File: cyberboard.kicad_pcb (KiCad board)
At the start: 4 copper layers, 65 x 56.5 mm, 51 parts, among them J1 Conn_01x02, J2 Conn_01x06, J3 5024940670, J4 Lidar, J6 RPi_GPIO, J7 Conn_01x04, J8 Conn_01x03, Q1 AO3400A, Q2 AO3400A, Q3 AO3400A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

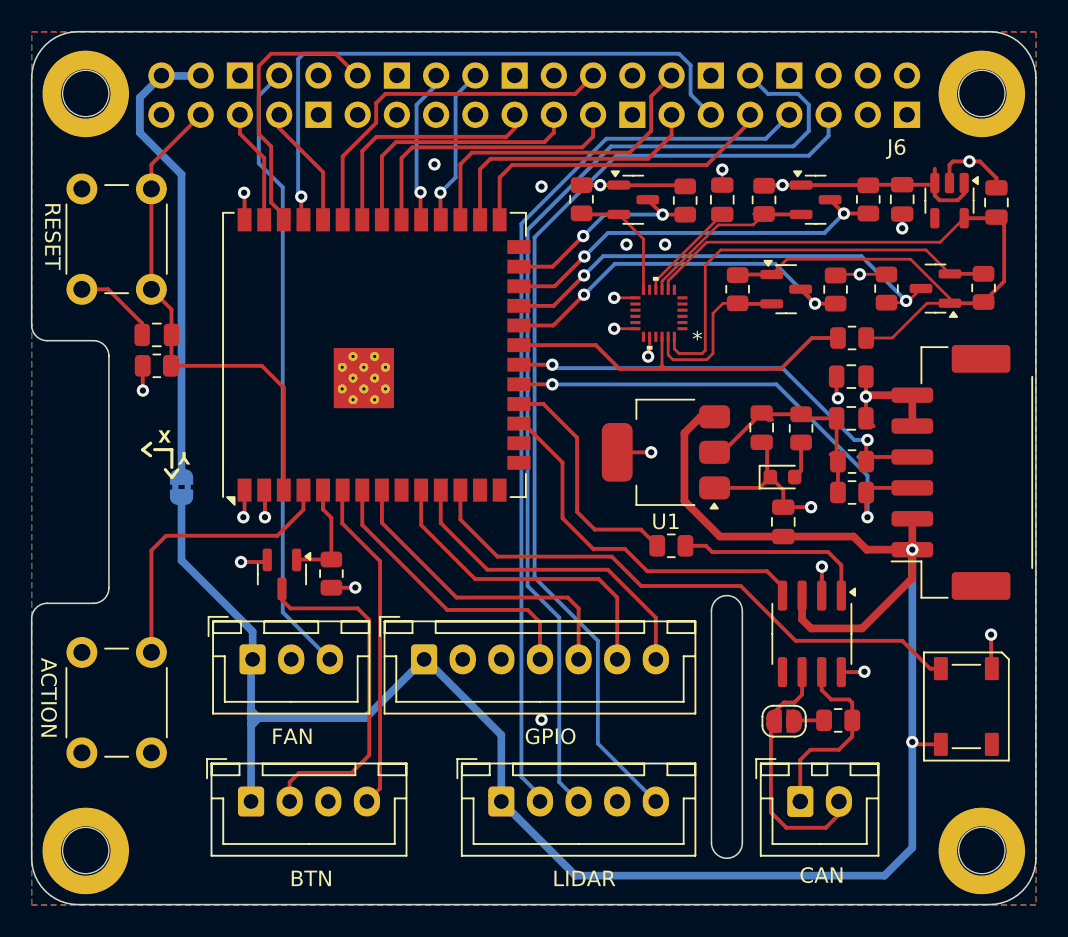
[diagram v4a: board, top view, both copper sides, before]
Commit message: add LED connector and update FAN connector
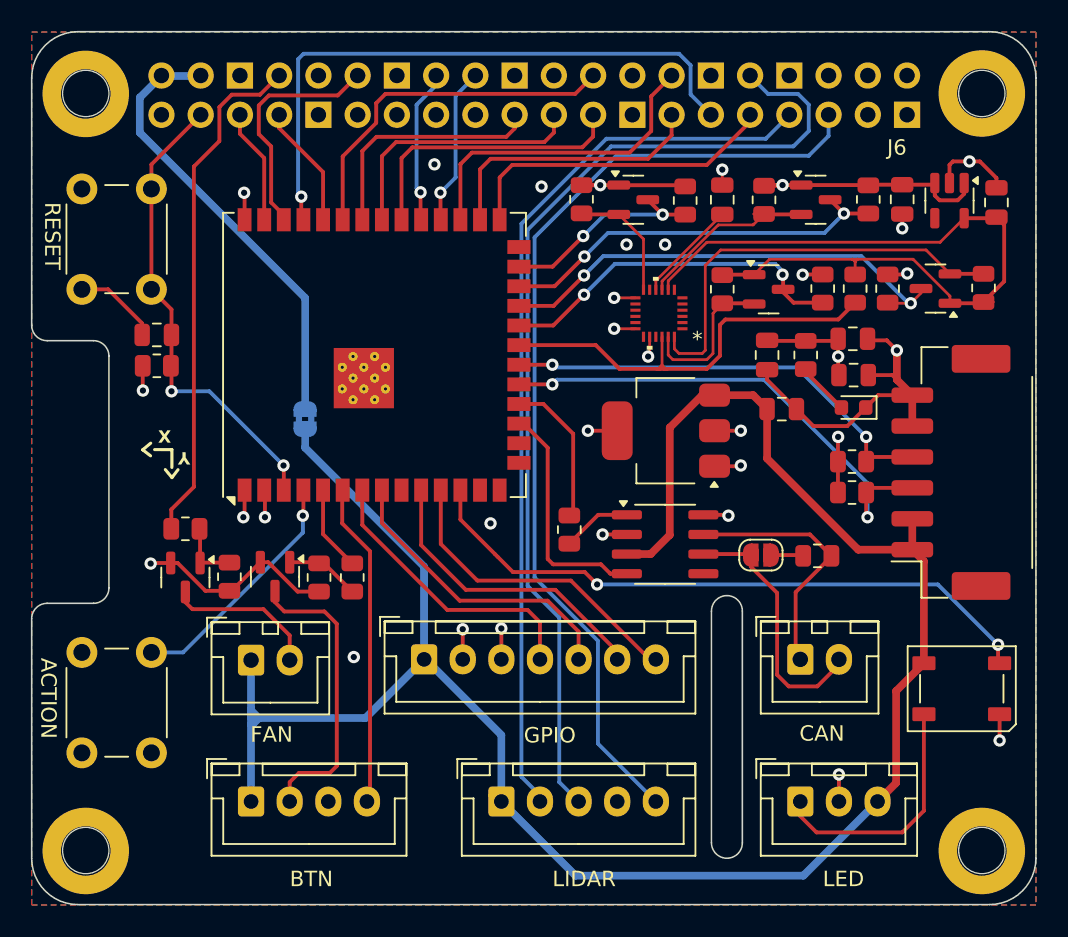
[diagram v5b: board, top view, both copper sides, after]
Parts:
- added J5: Conn_01x03, Connector_JST:JST_XH_B3B-XH-A_1x03_P2.50mm_Vertical, F.Cu at (156.0, 116.8)
- added Q6: AO3400A, Package_TO_SOT_SMD:SOT-23, F.Cu at (116.2, 102.3)
- added R6: 10k, Resistor_SMD:R_0805_2012Metric, F.Cu at (119.1, 102.3)
- added R7: 220, Resistor_SMD:R_0805_2012Metric, F.Cu at (116.2, 99.2)
- added R8: 220, Resistor_SMD:R_0805_2012Metric, F.Cu at (127.0, 102.3)
- J8: footprint Connector_JST:JST_XH_B3B-XH-A_1x03_P2.50mm_Vertical -> Connector_JST:JST_XH_B2B-XH-A_1x02_P2.50mm_Vertical
- moved U2 11.1 mm to (147.3, 100.2), turned to 0 degrees
- moved JP3 10.9 mm to (153.5, 100.9)
- moved R2 10.7 mm to (157.1, 100.9)
- moved J1 9.20 mm to (156.0, 107.6)
- moved JP1 9.13 mm to (124.0, 92.1)
- moved C3 7.30 mm to (154.8, 91.4), turned to 0 degrees
- moved R3 6.68 mm to (141.1, 99.2), turned to 90 degrees
- moved D2 6.44 mm to (159.5, 91.3), turned to 180 degrees
- moved R5 4.76 mm to (156.4, 87.9)
- moved C4 4.71 mm to (153.9, 87.9)
- moved R11 3.21 mm to (159.6, 83.6), turned to -90 degrees
- moved C2 2.80 mm to (159.5, 89.2)
- moved C6 2.45 mm to (159.4, 86.9)
- moved U1 1.40 mm to (147.3, 92.8)
- moved D1 1.19 mm to (166.5, 109.5), turned to 0 degrees
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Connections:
- D1 pad 2: unconnected-(D1-DOUT-Pad2) -> Net-(D1-DOUT)
- J6 pad 8: /FAN -> /FAN_PWM
- J8 pad 2: GND -> Net-(D3-A)
- Q4 pad 1: /BTN_LED -> Net-(Q4-G)
- R4 pad 2: /BTN_LED -> Net-(Q4-G)
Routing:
- net /FAN: track 40.2 -> 0.00 mm
- net /FAN_PWM: track 0.00 -> 33.3 mm
- net GND: track 47.7 -> 65.3 mm, vias 19 -> 21
- net Net-(D1-DOUT): track 0.00 -> 16.2 mm
- net Net-(D3-A): track 0.00 -> 9.90 mm
- net /CAN_RX: track 24.1 -> 15.2 mm
- net Net-(U2-TXD): track 12.6 -> 4.50 mm
- net /CAN_TX: track 15.9 -> 10.0 mm
- net Net-(Q4-G): track 0.00 -> 4.84 mm
- net +3.3V: track 53.0 -> 48.5 mm, vias 8 -> 12
- net /GPIO_LED: track 37.0 -> 41.3 mm, vias 0 -> 2
- net Net-(J1-Pin_1): track 12.3 -> 16.6 mm
- net Net-(Q6-G): track 0.00 -> 4.14 mm
- net +1V8: track 54.5 -> 50.7 mm
- net /BTN_LED_5V: track 22.8 -> 19.2 mm
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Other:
- board text added: "LED"

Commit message: fix pcb layout
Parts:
- added D3: D, Diode_SMD:D_SOD-323, F.Cu at (117.1, 106.4)
- moved R7 11.6 mm to (117.2, 87.6), turned to 90 degrees
- moved J7 0.91 mm to (121.4, 116.9)
- moved J8 0.91 mm to (121.4, 107.8)
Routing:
- net /FAN_PWM: track 33.3 -> 20.0 mm
- net Net-(Q6-G): track 4.14 -> 14.8 mm
- net +5V: track 135.9 -> 139.9 mm
- net Net-(D3-A): track 9.90 -> 11.4 mm
- net GND: track 65.3 -> 66.7 mm, vias 21 -> 20
- net /BTN_LED_5V: track 19.2 -> 17.8 mm
